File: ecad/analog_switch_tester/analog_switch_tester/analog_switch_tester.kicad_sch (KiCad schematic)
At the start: 10 parts, among them J1 Conn_01x08_Pin, U1 DRV5056A1xQDBZxR, U2 CD4051B, U3 DRV5056A2xQDBZxR, U4 DRV5056A3xQDBZxR, U5 DRV5056A4xQDBZxR

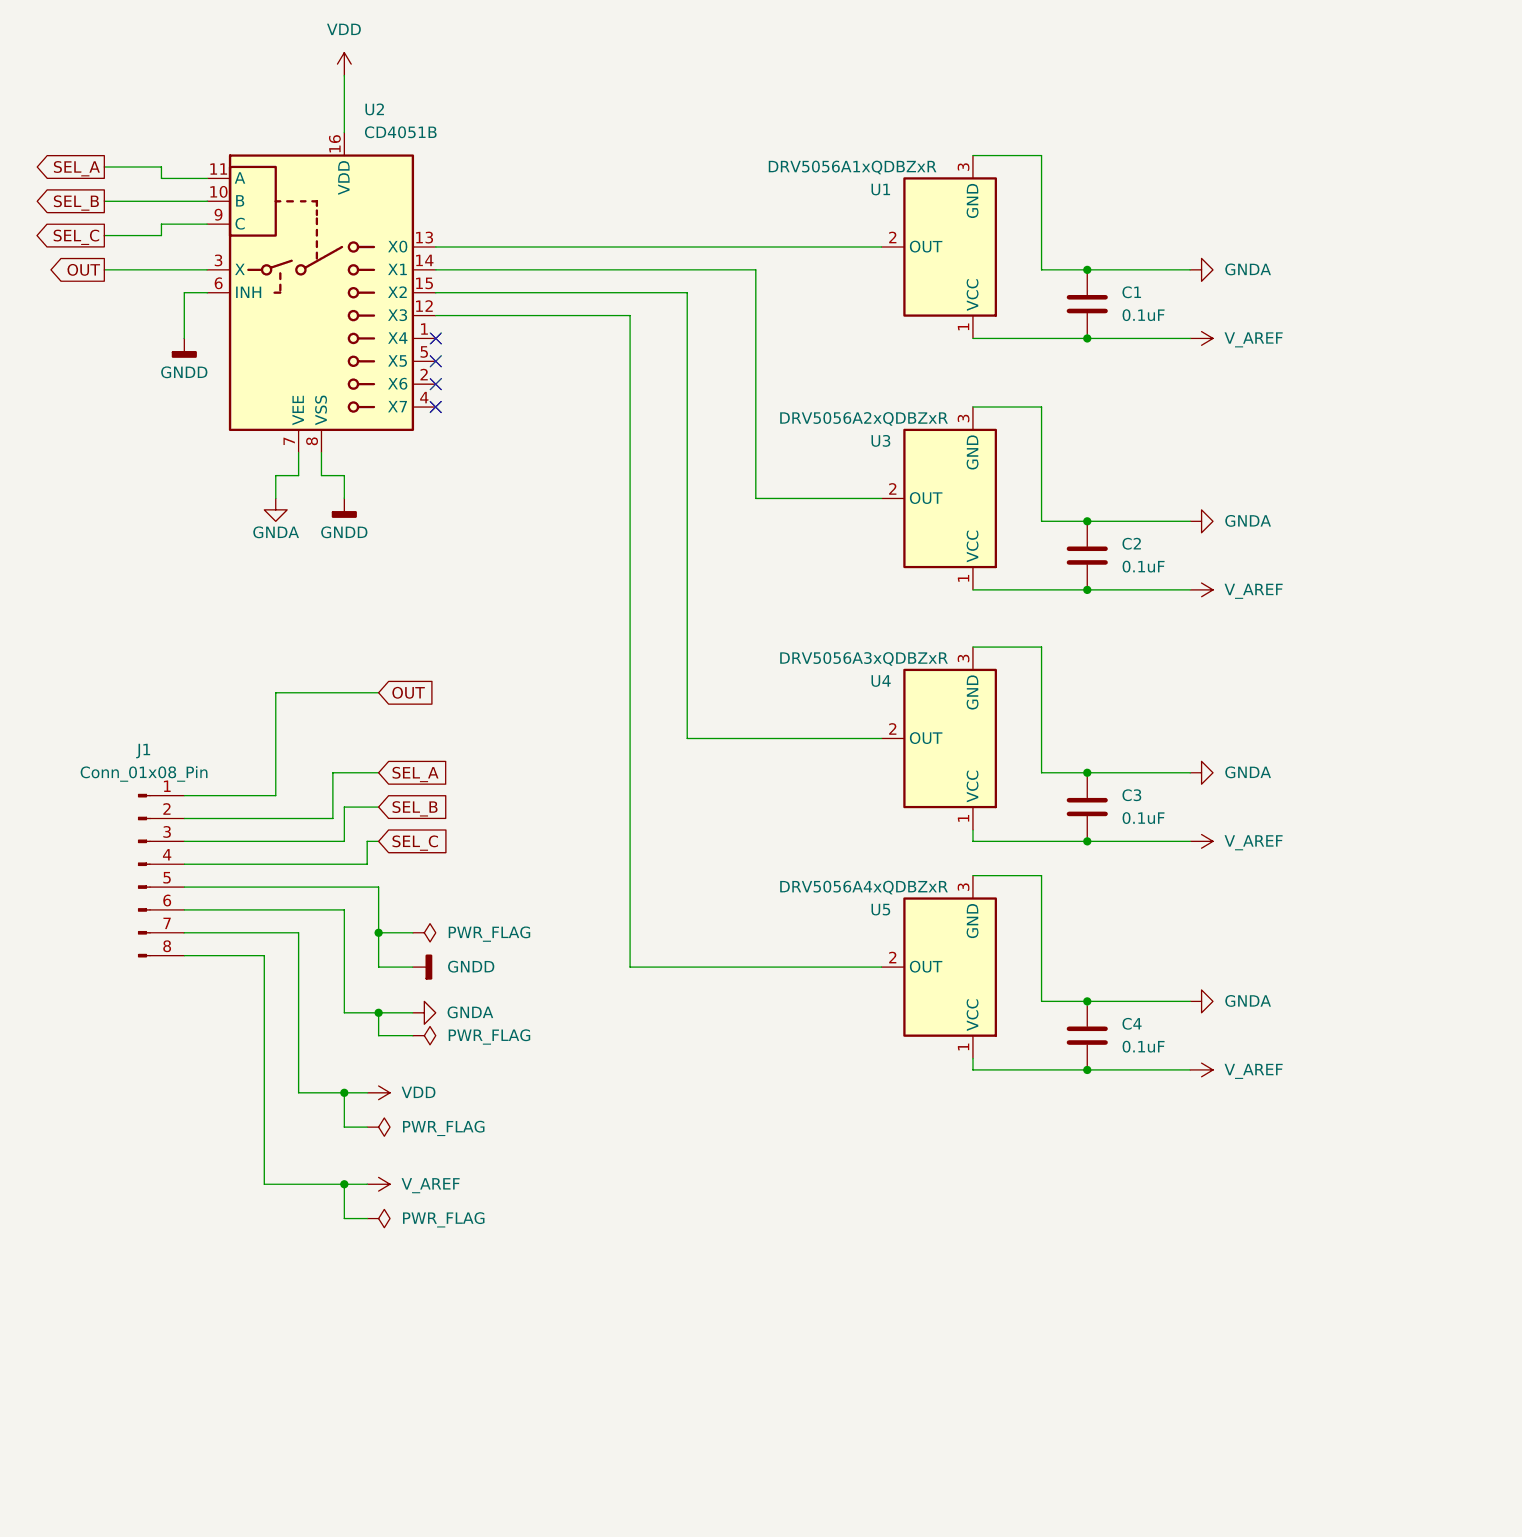
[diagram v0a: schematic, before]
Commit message: Add low-pass filters
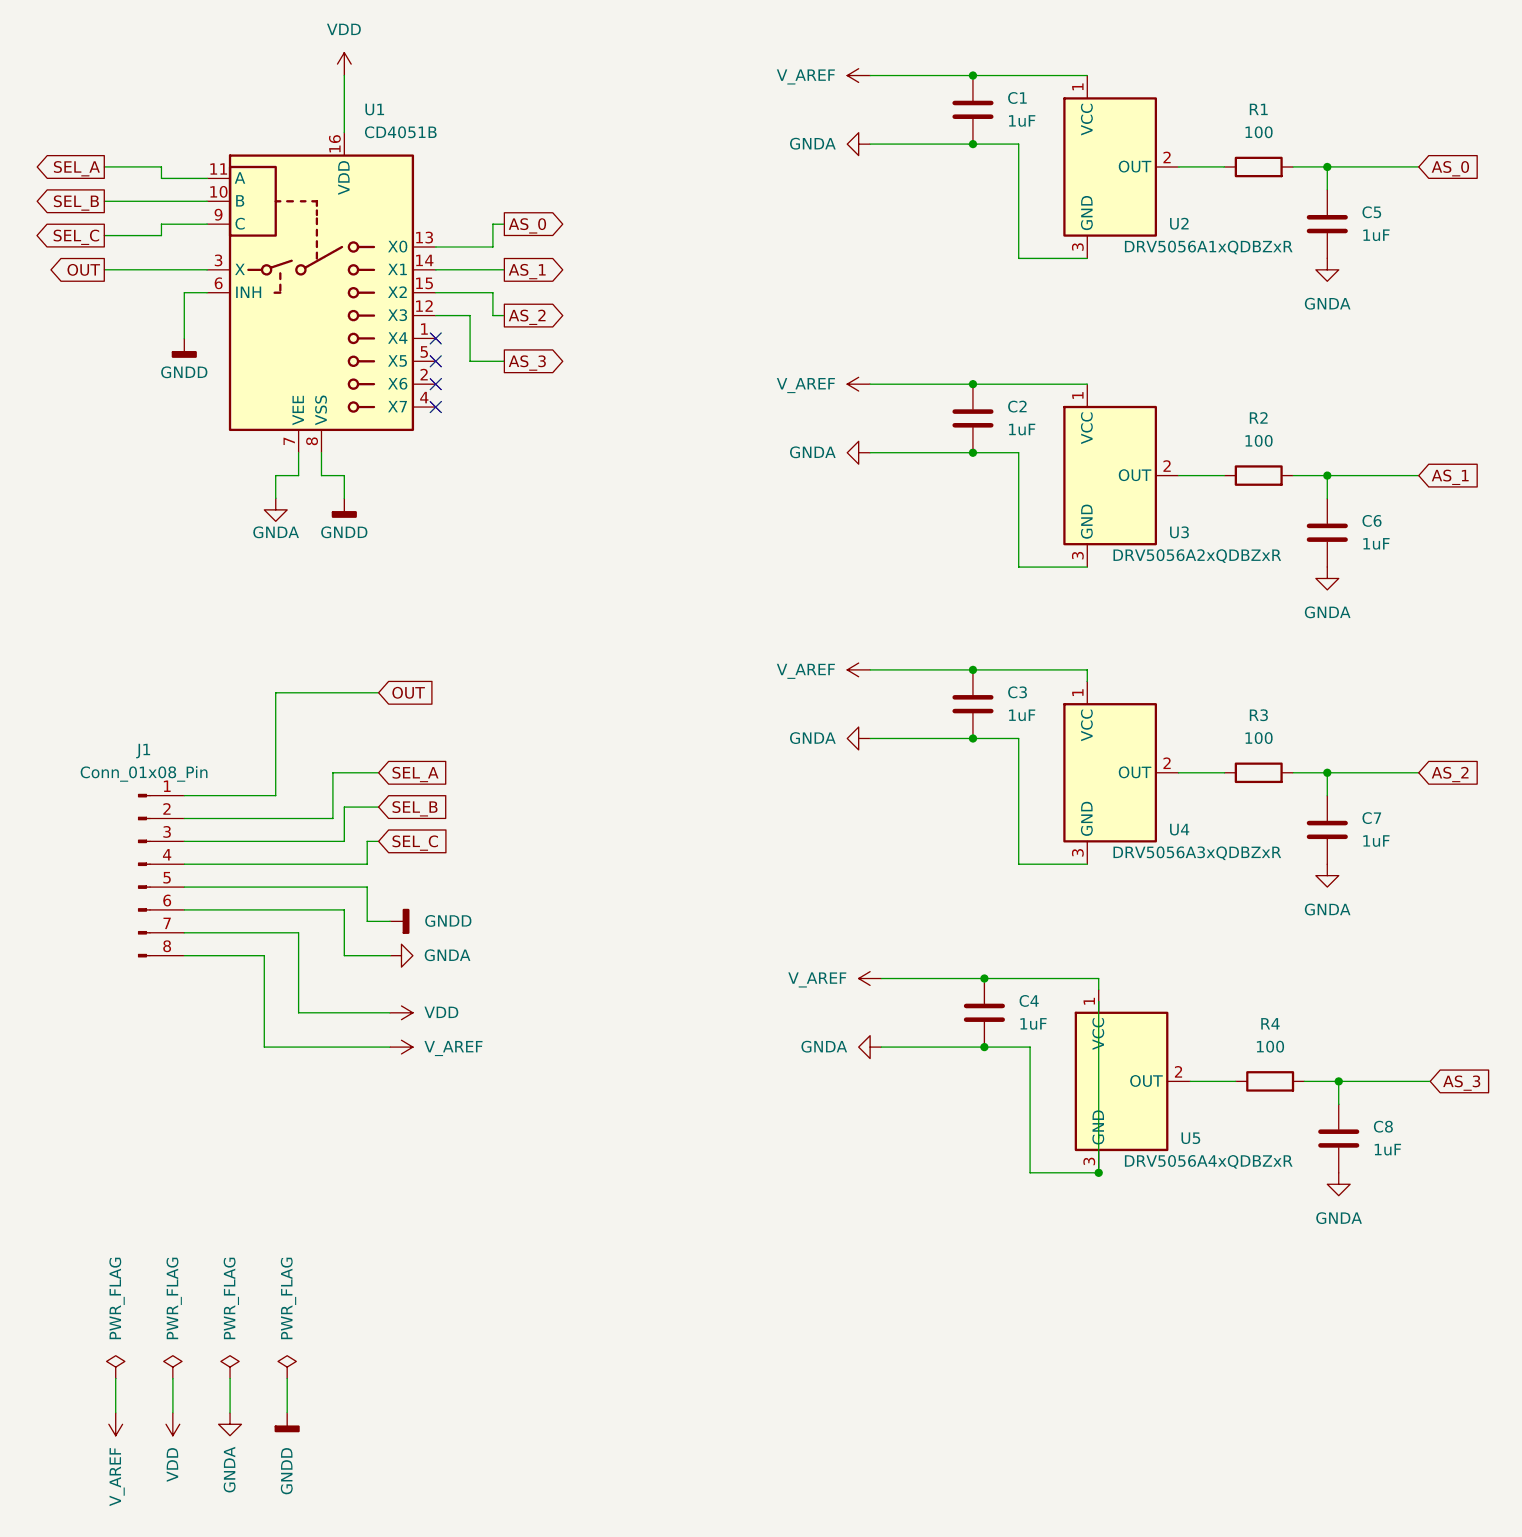
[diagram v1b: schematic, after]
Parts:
- removed U1: DRV5056A1xQDBZxR, Package_TO_SOT_SMD:SOT-23, symbol udong_library:DRV5056A1xQDBZxR
- added C5, C6, C7, C8: 1uF, Capacitor_SMD:C_0603_1608Metric, symbol Device:C
- added R1, R2, R3, R4: 100, Resistor_SMD:R_0603_1608Metric, symbol Device:R
- added U2: DRV5056A1xQDBZxR, Package_TO_SOT_SMD:SOT-23, symbol udong_library:DRV5056A1xQDBZxR
- C1, C2, C3, C4: value 0.1uF -> 1uF
- renumbered U2 to U1
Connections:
- net GNDA: now also C5.1, C6.1, C7.1, C8.1, U2.3 (GND)
- net V_AREF: now also U2.1 (VCC)
- net AS_0: now reaches U1.13 (X0)
- net AS_0: now also C5.2, R1.2
- net at U5.2 (OUT): now also R4.1; no longer U1.12 (X3)
- net at U3.2 (OUT): now also R2.1; no longer U1.14 (X1)
- net at U4.2 (OUT): now also R3.1; no longer U1.15 (X2)
- new net: R1.1, U2.2 (OUT)
- new net AS_1: C6.2, R2.2, U1.14 (X1)
- new net AS_2: C7.2, R3.2, U1.15 (X2)
- new net AS_3: C8.2, R4.2, U1.12 (X3)
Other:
- moved on the sheet: C2, C3, C4, U3, U4, U5

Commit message: .
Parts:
- removed C2, C3, C4: 1uF, symbol Device:C
- removed C6, C7, C8: 1uF, Capacitor_SMD:C_0603_1608Metric, symbol Device:C
- removed J1: Conn_01x08_Pin, Connector_JST:JST_EH_B8B-EH-A_1x08_P2.50mm_Vertical, symbol Connector:Conn_01x08_Pin
- removed R2, R3, R4: 100, Resistor_SMD:R_0603_1608Metric, symbol Device:R
- removed U1: CD4051B, Package_DIP:DIP-16_W7.62mm, symbol Analog_Switch:CD4051B
- removed U3: DRV5056A2xQDBZxR, Package_TO_SOT_SMD:SOT-23, symbol udong_library:DRV5056A2xQDBZxR
- removed U4: DRV5056A3xQDBZxR, Package_TO_SOT_SMD:SOT-23, symbol udong_library:DRV5056A3xQDBZxR
- removed U5: DRV5056A4xQDBZxR, Package_TO_SOT_SMD:SOT-23, symbol udong_library:DRV5056A4xQDBZxR
- added J1: Conn_01x03_Pin, Connector_PinHeader_1.00mm:PinHeader_1x03_P1.00mm_Horizontal, symbol Connector:Conn_01x03_Pin
- C1: footprint (none) -> Capacitor_SMD:C_0603_1608Metric
- U1: renamed from U2; footprint Package_TO_SOT_SMD:SOT-23 -> Udong:SW_Cherry_MX_PCB_1.00u_hall_effect
- renumbered C5 to C2
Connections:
- net AS_0 is gone; now on net OUT: C2.2, R1.2
- net GNDA: now also J1.3 (Pin_3)
- net OUT: now also J1.1 (Pin_1)
- net V_AREF: now also J1.2 (Pin_2)
- no-connect marks 4 -> 0
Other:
- moved on the sheet: C1, C2, R1, U1

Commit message: .
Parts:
- J1: footprint Connector_PinHeader_1.00mm:PinHeader_1x03_P1.00mm_Horizontal -> Connector_PinHeader_2.54mm:PinHeader_1x03_P2.54mm_Vertical
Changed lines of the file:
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@@
 			)
 		)
-		(property "Footprint" "Connector_PinHeader_1.00mm:PinHeader_1x03_P1.00mm_Horizontal"
+		(property "Footprint" "Connector_PinHeader_2.54mm:PinHeader_1x03_P2.54mm_Vertical"
 			(at 21.59 55.88 0)
 			(effects

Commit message: .
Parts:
- added Mount: Conn_01x03_Pin, Connector_PinHeader_2.54mm:PinHeader_1x03_P2.54mm_Vertical, symbol Connector:Conn_01x03_Pin
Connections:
- no-connect marks 0 -> 3
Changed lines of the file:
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@@
 		(color 0 0 0 0)
+	)
+	(no_connect
+		(at 60.96 67.31)
+	)
+	(no_connect
+		(at 60.96 72.39)
+	)
+	(no_connect
+		(at 60.96 69.85)
 	)
 	(wire
@@
 					(unit 1)
 				)
+			)
+		)
+	)
+	(symbol
+		(lib_id "Connector:Conn_01x03_Pin")
+		(at 55.88 69.85 0)
+		(unit 1)
+		(exclude_from_sim no)
+		(in_bom yes)
+		(on_board yes)
+		(dnp no)
+		(fields_autoplaced yes)
+		(property "Reference" "Mount"
+			(at 56.515 62.23 0)
+			(effects
+				(font
+					(size 1.27 1.27)
+				)
+			)
+		)
+		(property "Value" "Conn_01x03_Pin"
+			(at 56.515 64.77 0)
+			(effects
+				(font
+					(size 1.27 1.27)
+				)
+			)
+		)
+		(property "Footprint" "Connector_PinHeader_2.54mm:PinHeader_1x03_P2.54mm_Vertical"
+			(at 55.88 69.85 0)
+			(effects
+				(font
+					(size 1.27 1.27)
+				)
+				(hide yes)
+			)
+		)
+		(property "Datasheet" "~"
+			(at 55.88 69.85 0)
+			(effects
+				(font
+					(size 1.27 1.27)
+				)
+				(hide yes)
+			)
+		)
+		(property "Description" "Generic connector, single row, 01x03, script generated"
+			(at 55.88 69.85 0)
+			(effects
+				(font
+					(size 1.27 1.27)
+				)
+				(hide yes)
+			)
+		)
+		(pin "1"
+		)
+		(pin "3"
+		)
+		(pin "2"
+		)
+		(instances
+			(project "analog_switch_tester"
+				(path "/bc912bb6-7985-407f-bcee-658a2bff2f4b"
+					(reference "Mount")
+					(unit 1)
+				)

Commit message: .
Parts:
- renumbered Mount to Mount1
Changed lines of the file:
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@@
 		(dnp no)
 		(fields_autoplaced yes)
-		(property "Reference" "Mount"
+		(property "Reference" "Mount1"
 			(at 56.515 62.23 0)
 			(effects
@@
 			(project "analog_switch_tester"
 				(path "/bc912bb6-7985-407f-bcee-658a2bff2f4b"
-					(reference "Mount")
+					(reference "Mount1")
 					(unit 1)
 				)
